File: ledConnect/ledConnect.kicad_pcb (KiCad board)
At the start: 2 copper layers, 43.9 x 43.9 mm, 22 parts, among them Q1 AO4407A, SW1 SS-12M11G5, U1 MT30-M, U2 TPS565208DDCR

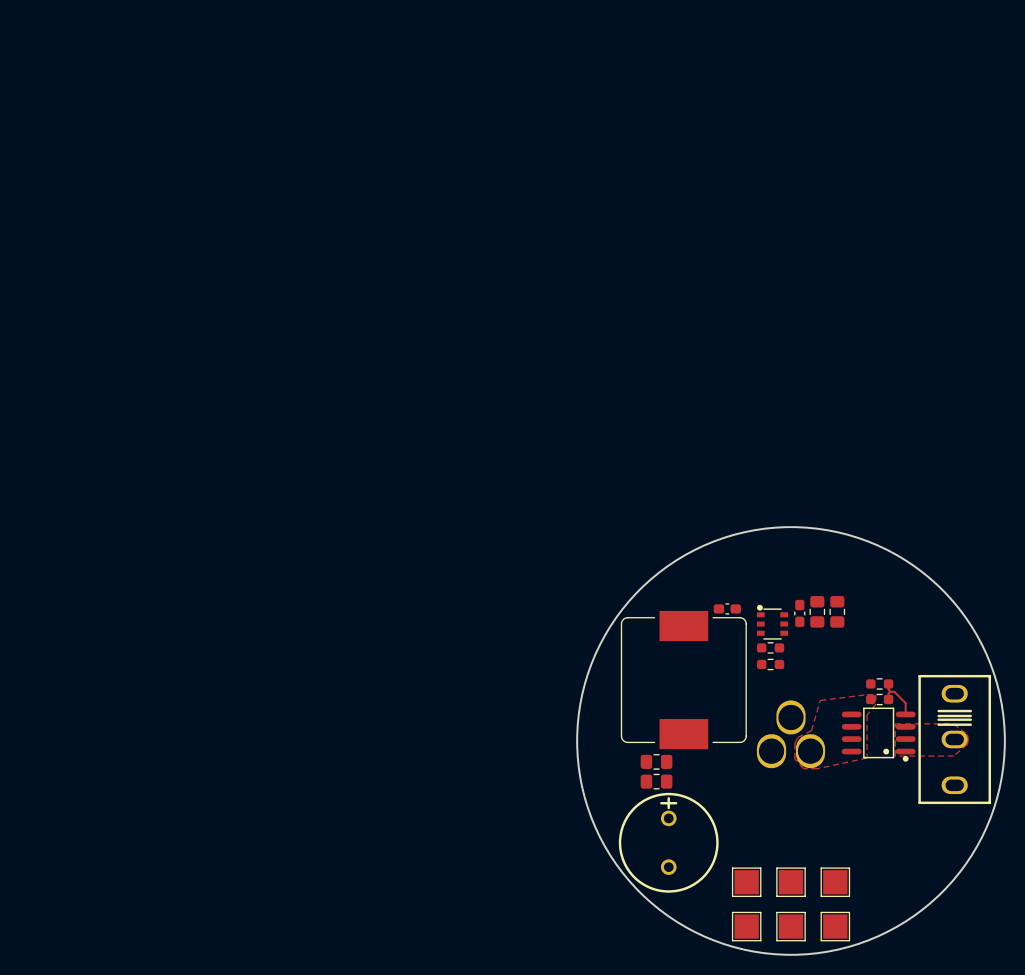
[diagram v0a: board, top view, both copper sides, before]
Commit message: via stiching fehlt noch
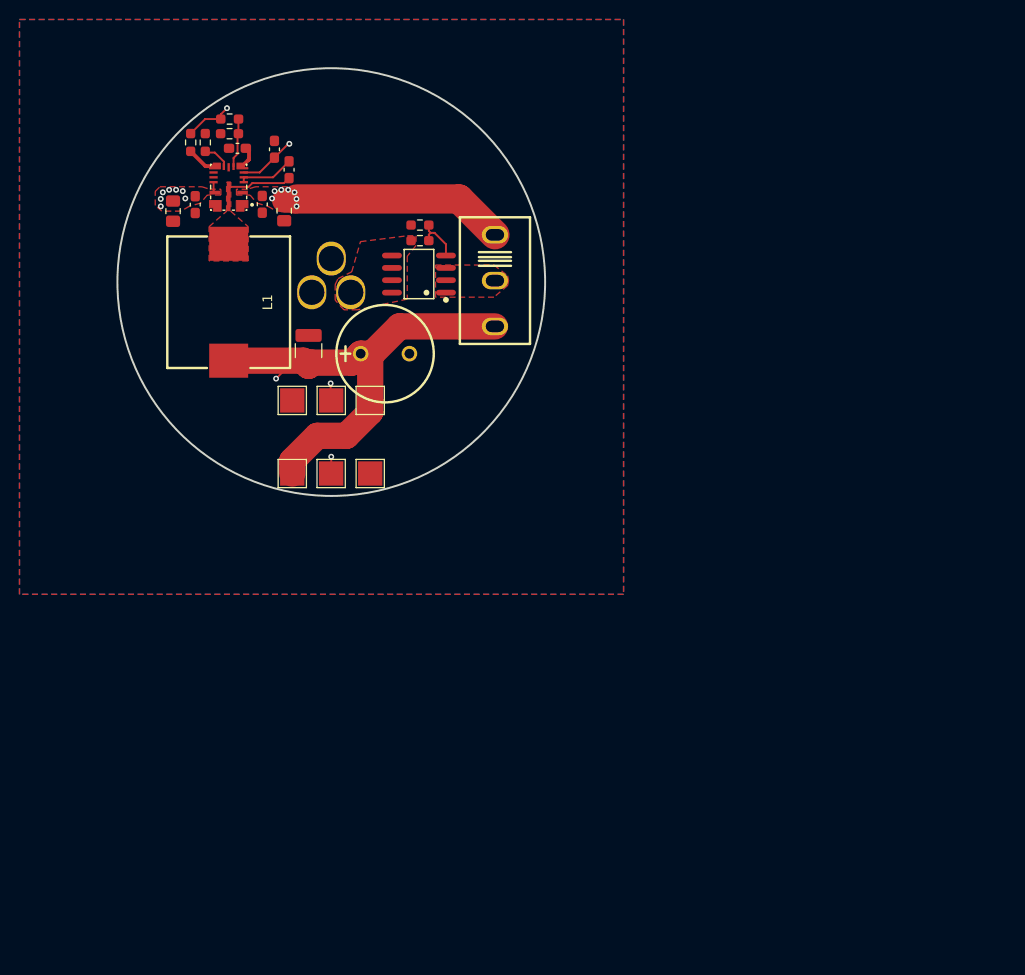
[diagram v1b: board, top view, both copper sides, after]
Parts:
- removed C2, C6: 10uF, Capacitor_SMD:C_0805_2012Metric_Pad1.18x1.45mm_HandSolder
- removed C3, C4: 100nF, Capacitor_SMD:C_0603_1608Metric_Pad1.08x0.95mm_HandSolder
- removed C5, C7: 22uF, Capacitor_SMD:C_0805_2012Metric_Pad1.18x1.45mm_HandSolder
- added Cbias1: 100nF, Capacitor_SMD:C_0603_1608Metric_Pad1.08x0.95mm_HandSolder, F.Cu at (147.0, 79.2)
- added Cboot1: 100nF, Capacitor_SMD:C_0603_1608Metric_Pad1.08x0.95mm_HandSolder, F.Cu at (148.5, 81.3)
- added Cin1: 10uF, Capacitor_SMD:C_0805_2012Metric_Pad1.18x1.45mm_HandSolder, F.Cu at (148.0, 85.5)
- added Cin2: 10uF, Capacitor_SMD:C_0805_2012Metric_Pad1.18x1.45mm_HandSolder, F.Cu at (136.6, 85.6)
- added Cinx1: 1uF, Capacitor_SMD:C_0603_1608Metric_Pad1.08x0.95mm_HandSolder, F.Cu at (145.7, 84.9)
- added Cinx2: 1uF, Capacitor_SMD:C_0603_1608Metric_Pad1.08x0.95mm_HandSolder, F.Cu at (138.9, 84.9)
- added Cout1: 47uF, Capacitor_SMD:C_1210_3225Metric_Pad1.33x2.70mm_HandSolder, F.Cu at (150.5, 99.9)
- added Cvcc1: 1uF, Capacitor_SMD:C_0603_1608Metric_Pad1.08x0.95mm_HandSolder, F.Cu at (143.2, 79.1)
- added Rreset1: 100k, Resistor_SMD:R_0603_1608Metric_Pad0.98x0.95mm_HandSolder, F.Cu at (138.4, 78.5)
- added Rt1: 53.6k, Resistor_SMD:R_0603_1608Metric_Pad0.98x0.95mm_HandSolder, F.Cu at (139.9, 78.5)
- L1: value 3.3uH -> 15uH; footprint Inductor_SMD:L_TaiTech_TMPC1265_13.5x12.5mm -> easyeda2kicad:IND-SMD_L13.5-W12.6
- Rfbb1: value 10k -> 9.09k
- Rfbt1: value 54.9k -> 100k
- U2: value TPS565208DDCR -> LM61480RPHR; footprint easyeda2kicad:TSOT-23-6_L2.9-W1.6-P0.95-LS2.8-BR -> easyeda2kicad:VQFN-16_L4.5-W3.5-P0.50-TL_TI_RPH
- moved Rfbt1 78.8 mm to (142.4, 76.1), turned to 180 degrees
- moved Rfbb1 76.6 mm to (142.4, 77.6), turned to 0 degrees
- moved U2 71.7 mm to (142.3, 83.0)
- moved TP5 71.6 mm to (152.8, 105.0)
- moved TP4 69.1 mm to (156.8, 105.0)
- moved TP1 68.0 mm to (148.8, 105.0)
- moved SW1 66.7 mm to (169.6, 92.7)
- moved U1 66.7 mm to (152.8, 92.2)
- moved Q1 66.7 mm to (161.8, 92.0)
- moved R1 66.7 mm to (161.9, 88.6)
- moved R2 66.7 mm to (161.9, 87.0)
- moved TP6 66.6 mm to (156.8, 112.5)
- moved TP3 66.2 mm to (148.8, 112.5)
- moved TP2 63.1 mm to (152.8, 112.5)
- moved L1 60.7 mm to (142.3, 94.9)
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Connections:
- net +12V renamed VIN
- Rfbb1 pad 1: Net-(U2-VFB) -> GND
- Rfbb1 pad 2: GND -> FB
- Rfbt1 pad 1: VDC -> FB
- Rfbt1 pad 2: Net-(U2-VFB) -> VDC
- SW1 pad 1: EN -> VIN2
- U2 pad 2: Net-(U2-SW) -> VIN2
- U2 pad 3: EN -> CBOOT
- U2 pad 4: Net-(U2-VFB) -> CBOOT
- U2 pad 5: EN -> VDC
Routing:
- net VDC: track 0.00 -> 169.7 mm, vias 0 -> 3
- net VIN2: track 0.00 -> 24.3 mm, vias 0 -> 14
- net LED_DATA: track 0.00 -> 23.9 mm, vias 0 -> 2
- net Net-(U2-SW): track 0.00 -> 8.41 mm
- net CBOOT: track 0.00 -> 5.83 mm
- net FB: track 0.00 -> 5.09 mm
- net Net-(U2-~{RESET}): track 0.00 -> 3.13 mm
- net Net-(U2-RT): track 0.00 -> 2.86 mm
- net Net-(U2-VCC): track 0.00 -> 2.37 mm
- added copper zone on B.Cu, net GND
- added copper zone on F.Cu, net GND
- added copper zone on In1.Cu, net GND
- added copper zone on In2.Cu, net GND
- added copper zone on F.Cu, net Net-(U2-SW)
- added copper zone on F.Cu, net VIN2
- added copper zone on In1.Cu, net VIN2
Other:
- copper layers 2 -> 4

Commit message: bestelle teile
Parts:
- moved Rreset1 1.48 mm to (138.4, 80.0)
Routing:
- net VDC: track 169.7 -> 171.2 mm
- net Net-(U2-~{RESET}): track 3.13 -> 2.52 mm
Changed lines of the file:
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@@
 	(footprint "Resistor_SMD:R_0603_1608Metric_Pad0.98x0.95mm_HandSolder"
 		(layer "F.Cu")
-		(at 138.3825 78.52 90)
+		(at 138.3825 80 90)
 		(descr "Resistor SMD 0603 (1608 Metric), square (rectangular) end terminal, IPC-7351 nominal with elongated pad for handsoldering. (Body size source: IPC-SM-782 page 72, https://www.pcb-3d.com/wordpress/wp-content/uploads/ipc-sm-782a_amendment_1_and_2.pdf), generated with kicad-footprint-generator")
 		(tags "resistor handsolder")
@@
 				(type solid)
 			)
-			(layer "F.SilkS")
-		)
-		(fp_circle
-			(center 0 0)
-			(end 5 0)
-			(stroke
-				(width 0.25)
-				(type solid)
-			)
-			(fill no)
 			(layer "F.SilkS")
 		)
@@
 	)
 	(segment
+		(start 139.88 76.12)
+		(end 138.3825 77.6175)
+		(width 0.2)
+		(layer "F.Cu")
+		(net 2)
+	)
+	(segment
 		(start 148.4575 101.4525)
 		(end 150.4825 101.4525)
@@
 	)
 	(segment
+		(start 138.3825 77.6175)
+		(end 138.3825 79.0875)
+		(width 0.2)
+		(layer "F.Cu")
+		(net 2)
+	)
+	(segment
 		(start 141.47 76.12)
 		(end 141.47 75.64)
@@
 	)
 	(segment
+		(start 141.47 76.12)
+		(end 139.88 76.12)
+		(width 0.2)
+		(layer "F.Cu")
+		(net 2)
+	)
+	(segment
 		(start 141.47 75.64)
 		(end 142.11 75)
-		(width 0.2)
-		(layer "F.Cu")
-		(net 2)
-	)
-	(segment
-		(start 139.87 76.12)
-		(end 141.47 76.12)
 		(width 0.2)
 		(layer "F.Cu")
@@
 		(end 154.9125 101.12)
 		(width 2.7)
-		(layer "F.Cu")
-		(net 2)
-	)
-	(segment
-		(start 138.3825 77.6075)
-		(end 139.87 76.12)
-		(width 0.2)
 		(layer "F.Cu")
 		(net 2)
@@
 	)
 	(segment
+		(start 139.8625 80.9125)
+		(end 138.3825 80.9125)
+		(width 0.4)
+		(layer "F.Cu")
+		(net 12)
+	)
+	(segment
 		(start 139.9 80.95)
-		(end 138.3825 79.4325)
+		(end 139.8625 80.9125)
 		(width 0.4)
 		(layer "F.Cu")

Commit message: kurz vor bestellung
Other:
- board text added: "Janek"
- board text added: "github.com/janekc"
